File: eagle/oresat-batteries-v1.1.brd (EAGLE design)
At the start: 98.6 x 95.3 mm, 104 parts, among them IC1 74AHC1G08DBV, U1 TCAN330, U10 LTC4412, U2 STM32F042K6, U3 LTC4411, U4 LTC4411, U5 LTC4411, U6 LTC4411, U7 LTC4412, U8 LTC4412, U9 LTC4412, X1 16MHz

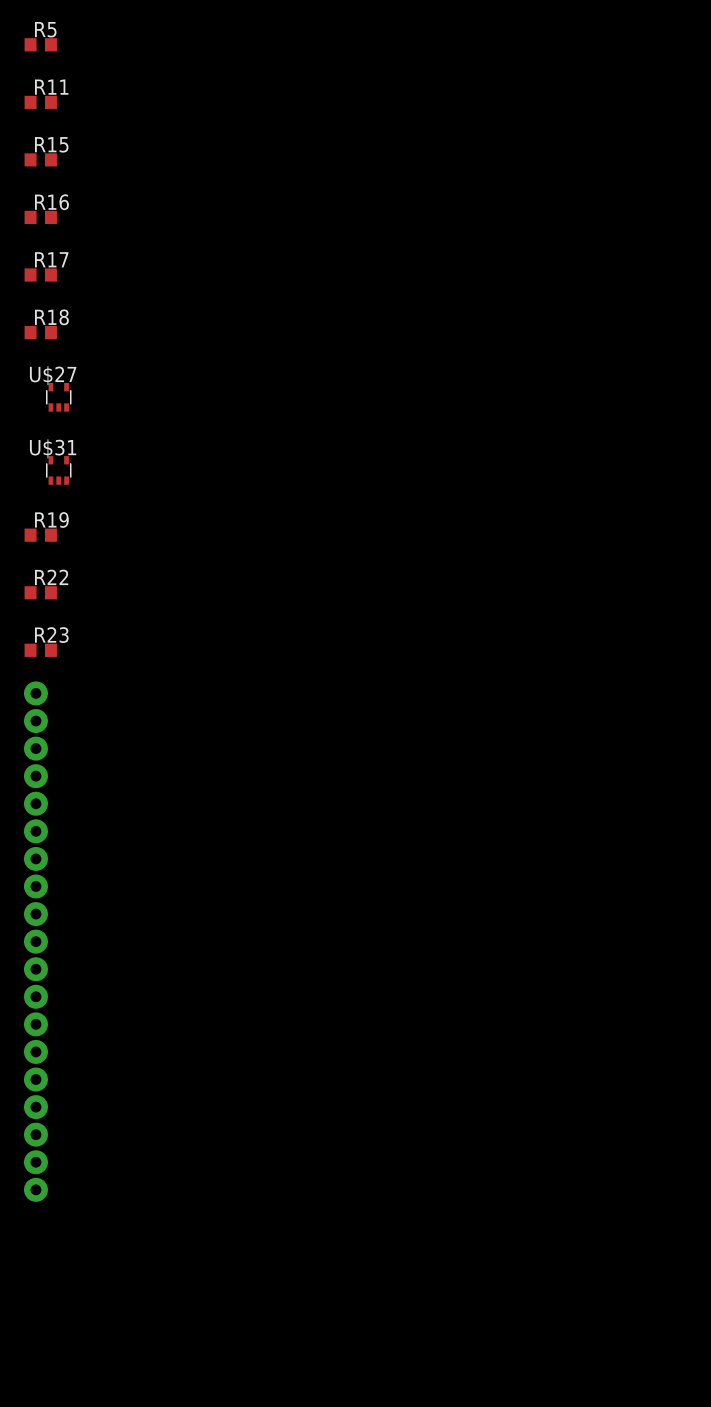
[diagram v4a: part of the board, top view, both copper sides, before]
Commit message: Added double pin header.
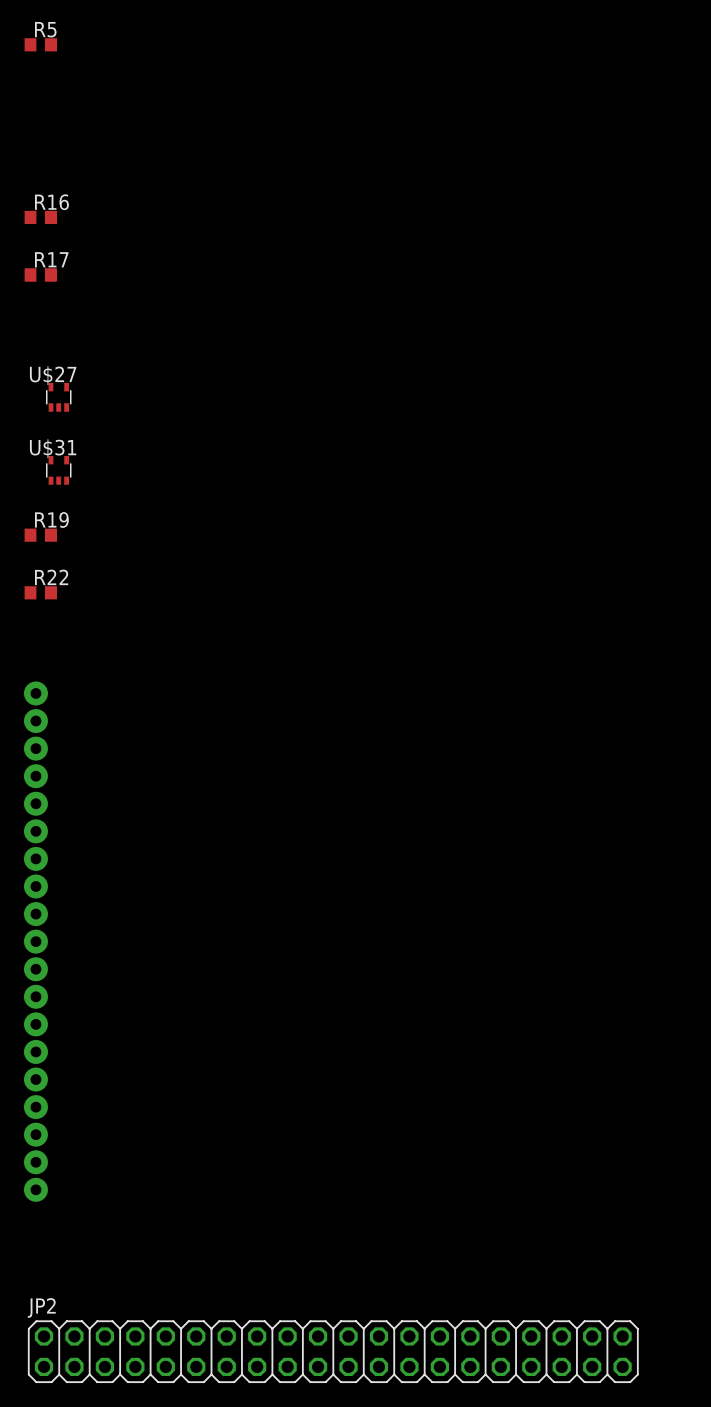
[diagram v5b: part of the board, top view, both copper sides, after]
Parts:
- removed R11, R15, R18, R23: 470k, rcl:R0603
- added JP2: (no value), pinhead:2X20
- R8, R9: value 1.6k -> 4.7k
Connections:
- removed net LOWSHD: C1.1, CF1.11, IC1.1, R14.2, R7.1, U$2.5, U$26.P$1, U$4.P$1
- removed net N$6: C14.1, IC1.5, R14.1
- removed net U10STAT: R5.2, U10.4, U2.26
- removed net U4STAT: R17.2, U2.12, U4.4
- removed net U5STAT: R18.2, U2.13, U5.4
- removed net U8STAT: R4.2, U2.27, U8.4
- new net N$4: U2.18
- new net SPARE1: CF1.19, CF1.20, JP2.19
- new net SPARE10: CF1.37, CF1.38, JP2.37
- new net SPARE11: CF1.39, CF1.40, JP2.39
- new net SPARE2: CF1.21, CF1.22, JP2.21
- new net SPARE3: CF1.23, CF1.24, JP2.23
- new net SPARE4: CF1.25, CF1.26, JP2.25
- new net SPARE5: CF1.27, CF1.28, JP2.27
- new net SPARE6: CF1.29, CF1.30, JP2.29
- new net SPARE7: CF1.31, CF1.32, JP2.31
- new net SPARE8: CF1.33, CF1.34, JP2.33
- new net SPARE9: CF1.35, CF1.36, JP2.35
- new net SYSSHD: C1.1, CF1.17, CF1.18, IC1.1, JP2.17, JP2.18, R14.2, R7.1, U$2.5, U$26.P$1, U$4.P$1
- net 3V3: no longer R11.1, R15.1, R18.1, R23.1
- net BATT+: now also C14.1, IC1.5, R14.1
- net BATT-: no longer R2.1
- net CANH: now also CF1.3, CF1.4, JP2.3, JP2.4; no longer CF1.2
- net CANL: now also CF1.2, JP2.1, JP2.2
- net CHG_CTL: now also CF1.13, CF1.14, JP2.13, JP2.14; no longer CF1.7
- net C_SENSE: now also R2.1, R6.2
- net DCHG_CTL: now also CF1.15, CF1.16, JP2.15, JP2.16; no longer CF1.9
- net GND: now also CF1.11, CF1.12, CF1.5, CF1.6, JP2.11, JP2.5; no longer R6.2
- net U3STAT: now also R17.2, U2.12, U4.4; no longer R23.2, U2.18
- net U6STAT: now also U5.4
- net U7STAT: now also R5.2, U10.4, U2.26; no longer R15.2, U2.10
- net U9STAT: now also R4.2, U2.27, U8.4; no longer R11.2, U2.15
- net VSOLAR: now also CF1.10, CF1.7, CF1.8, CF1.9, JP2.6, JP2.7, JP2.8, JP2.9; no longer CF1.3, CF1.4, CF1.5, CF1.6

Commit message: Fixed most of the issues from design review Sept 25.
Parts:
- removed C16, C17: 10u, rcl:C0805
- removed DEBUG_DNP: (no value), pinhead:2X08
- removed R21, R22: 10k, rcl:R0603
- removed U$1: LM3761, oresat-batteries:SOT23-5
- removed U$2: BQ2970, oresat-batteries:PSOP6
- removed U$21: 4.19, oresat-batteries:RES_HEATER
- removed U$27, U$31: MC74HC1G04DFT1GOSCT, MC74HC1G04DFT1GOSCT:SC70-5
- removed U$49: TP, oresat-batteries:2MM_TP
- added C4, C7: .1u, rcl:C0603
- added D1, D2, D3: CMDD6001, CMMDD6001:SOD323
- added JP1: (no value), pinhead:2X20
- added R11: 4.7k, rcl:R0603
- added R15, R18: 470k, rcl:R0603
- added TP6: TP, oresat-batteries:2MM_TP
- added U12, U13: LTC4412, ltc4412:SOT23-6
- added U14: STM32F042K6, oresat-batteries:QFP32-7X7
- added U15: TCAN330, oresat-batteries:SOT23-8_TI-DCN
- C1, C3: value .1u -> 10u; device rcl:C0603 -> rcl:C0805
- C10, C11: value 100n -> 20p
- C14: value .1u -> 100n
- C15: value 10u -> 100n; device rcl:C0805 -> rcl:C0603
- C2: value .47u -> 10u; device rcl:C0603 -> rcl:C0805
- C8: value 20p -> .1u
- C9: value 20p -> .47u
- JP2: device pinhead:2X20 -> pinhead:2X08
- R1: value 10k -> 330
- R12: value 10k -> 4.7k
- R13: value DNP/0 -> 10k
- R14: value 2.2k -> 470k
- R16: value 470k -> DNP/0
- R20: value 10k -> 4.19; device rcl:R0603 -> oresat-batteries:RES_HEATER
- R3: value .01-.05 -> 10k
- R4: value 470k -> 10k
- R5: value 470k -> 2.2k
- R7: value 330 -> .01-.05
- R8, R9: value 4.7k -> 10k
- U1: value TCAN330 -> LM3761; device oresat-batteries:SOT23-8_TI-DCN -> oresat-batteries:SOT23-5
- U2: value STM32F042K6 -> MC74HC1G04DFT1GOSCT; device oresat-batteries:QFP32-7X7 -> MC74HC1G04DFT1GOSCT:SC70-5
- U3: value LTC4411 -> BQ2970; device ltc4411:SOT23-5-B -> oresat-batteries:PSOP6
- U7: value LTC4412 -> LTC4411; device ltc4412:SOT23-6 -> ltc4411:SOT23-5-B
- U8: value LTC4412 -> MC74HC1G04DFT1GOSCT; device ltc4412:SOT23-6 -> MC74HC1G04DFT1GOSCT:SC70-5
- moved R8 294.6 mm to (-77.2, -210.5)
- moved R19 282.6 mm to (15.5, 56.5)
- moved U2 277.4 mm to (-75.7, -199.0)
- moved R16 273.7 mm to (28.5, 68.5)
- moved JP2 269.1 mm to (1.50, -15.0)
- moved R5 260.1 mm to (8.50, 76.0)
- moved C8 209.9 mm to (-71.1, -120.7)
- moved R14 206.7 mm to (-77.2, -164.8)
- moved R1 202.3 mm to (8.50, 79.0), turned to 180 degrees
- moved R9 197.7 mm to (-60.7, -115.9)
- moved R10 188.2 mm to (-60.7, -111.1)
- moved C9 186.1 mm to (-60.7, -106.3)
- moved U3 184.1 mm to (26.7, 77.3)
- moved R20 153.9 mm to (57.0, 51.0), flipped to the bottom
- moved C1 145.1 mm to (-28.9, -64.8)
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- renumbered C18 to C6, C19 to C5, CF1 to CM1, CF2 to J1, U$10 to TP15, U$11 to TP16, U$12 to TP31, U$13 to Q2, U$14 to Q1, U$15 to TP30, U$16 to TP3, U$17 to TP4, U$18 to TP13, U$19 to TP9, U$20 to Q7, U$22 to TP1, U$23 to TP2, U$24 to Q3, U$25 to TP18, U$26 to TP7, U$28 to TP8, U$29 to Q6, U$3 to B1, U$30 to Q4, U$32 to TP23, U$33 to TP24, U$34 to TP25, U$35 to TP26, U$36 to TP27, U$37 to TP28, U$38 to TP29, U$39 to TP22, U$4 to TP5, U$40 to TP21, U$41 to TP19, U$42 to TP34, U$43 to TP33, U$44 to TP20, U$45 to TP35, U$46 to TP14, U$47 to TP10, U$48 to TP11, U$5 to Q5, U$50 to TP12, U$6 to U11, U$8 to TP32, U$9 to TP17
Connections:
- removed net 3V3: C10.1, C11.1, C12.1, C13.1, C5.1, C6.1, DEBUG_DNP.1, DEBUG_DNP.2, J1.2, L1.1, Q7.P$5, Q7.P$6, Q7.P$7, Q7.P$8, Q7.P$9, R10.2, R16.1, R17.1, R4.1, R5.1, R8.2, R9.2, TP22.P$1, TP29.P$1, TP30.P$1, U$1.4, U1.3, U2.1, U2.17, U2.5
- removed net BATT+: B1.POS, C14.1, C15.1, C16.1, C3.1, IC1.5, Q3.5, Q3.6, Q3.7, Q3.8, Q4.5, Q4.6, Q4.7, Q4.8, R14.1, R19.2, R21.2, R22.2, R7.2, TP12.P$1, U$1.1, U$27.3, U$31.3, U11.10, U4.5, U6.5, U7.1, U9.1
- new net 3.3V: C12.1, C13.1, C14.1, C15.1, C5.1, C6.1, J1.2, JP2.1, JP2.2, L1.1, Q7.P$5, Q7.P$6, Q7.P$7, Q7.P$8, Q7.P$9, R11.2, R12.2, R13.2, R14.1, R15.1, R17.1, R18.1, TP22.P$1, TP29.P$1, TP30.P$1, U1.4, U14.1, U14.17, U14.5, U15.3
- new net N$10: D3.2, R4.1, U2.2
- new net N$6: D1.1, JP1.18
- new net N$9: D2.1, JP1.16
- new net VBATT: B1.POS, C1.1, C2.1, C7.1, C8.1, IC1.5, Q3.5, Q3.6, Q3.7, Q3.8, Q4.5, Q4.6, Q4.7, Q4.8, R1.2, R2.2, R4.2, R6.1, R8.2, TP12.P$1, U1.1, U10.1, U11.10, U2.3, U6.5, U7.5, U8.3, U9.1
- net 4411MB: now also U7.1; no longer U6.1
- net 4411_MT: now also U4.5, U6.1; no longer U3.5, U4.1
- net ALERT: now also R13.1, R16.2; no longer R10.1, R13.2
- net BATT-: now also U3.4; no longer U$2.4
- net BQVMIN: now also R5.1, U3.6; no longer R6.1, U$2.6
- net CANH: now also JP1.3, JP1.4, JP2.13, JP2.14, U15.7; no longer DEBUG_DNP.13, DEBUG_DNP.14, JP2.3, JP2.4, U1.7
- net CANL: now also JP1.1, JP1.2, JP2.11, JP2.12, U15.6; no longer DEBUG_DNP.11, DEBUG_DNP.12, JP2.1, JP2.2, U1.6
- net CAN_EN: now also U14.20, U15.5; no longer U1.5, U2.20
- net CAN_LSTN: now also U14.19, U15.8; no longer U1.8, U2.19
- net CAN_RX: now also U14.21, U15.4; no longer U1.4, U2.21
- net CAN_TX: now also U14.22, U15.1; no longer U1.1, U2.22
- net CHG_CTL: now also D3.1, JP1.13, JP1.14; no longer JP2.13, JP2.14, R22.1, U$27.2
- net CHG_SHD: now also U2.4, U7.3; no longer U$27.4, U3.3
- net COUT: now also U3.2; no longer U$2.2
- net C_SENSE: now also R5.2, R7.2, R9.1; no longer R2.1, R3.2, R6.2
- net DCHG_CTL: now also D2.2, JP1.15, R8.1, U8.2; no longer JP2.15, JP2.16, R19.1, U$31.2
- net DSCHG_SHD: now also U12.3, U13.3, U8.4; no longer U$31.4, U7.3, U8.3
- net GND: now also C4.2, C7.2, JP1.11, JP1.5, JP2.15, JP2.16, R19.1, R20.V-, R7.1, U12.2, U13.2, U14.16, U14.32, U15.2, U2.5, U8.5; no longer C16.2, C17.2, DEBUG_DNP.15, DEBUG_DNP.16, JP2.11, JP2.5, R12.1, R20.1, U$1.2, U$21.V-, U$27.5, U$31.5, U2.16, U2.32, U3.2, U8.2
- net HEAT: now also U14.7; no longer U2.7
- net N$1: now also U1.5; no longer U$1.5
- net N$11: now also U12.1, U9.6; no longer U10.1, U7.6
- net N$12: now also U9.5; no longer U7.5
- net N$13: now also R20.V+; no longer U$21.V+
- net N$16: now also U13.5; no longer U8.5
- net N$18: now also U10.6, U13.1; no longer U8.1, U9.6
- net N$19: now also U10.5; no longer U9.5
- net N$2: now also R19.2, U14.31; no longer R12.2, U2.31
- net N$3: now also R10.1, R9.2; no longer R1.1, R2.2
- net N$4: now also U14.18; no longer U2.18
- net N$5: now also U3.3; no longer U$2.3
- net N$7: now also C3.1, R2.1, R3.2, U1.3; no longer C17.1, R20.2, R21.1, U$1.3
- net N$8: now also U12.5; no longer U10.5
- net NRESET: now also U14.4; no longer U2.4
- net OSC_IN: now also C10.1, U14.2; no longer C8.1, U2.2
- net OSC_OUT: now also C11.1, U14.3; no longer C9.1, U2.3
- net REG: now also C9.1; no longer C2.1
- net SCL: now also R11.1, U14.29; no longer R8.1, U2.29
- net SDA: now also R12.1, U14.30; no longer R9.1, U2.30
- net SPARE1: now also JP1.19; no longer JP2.19
- net SPARE10: now also JP1.37; no longer JP2.37
- net SPARE11: now also JP1.39; no longer JP2.39
- net SPARE2: now also JP1.21; no longer JP2.21
- net SPARE3: now also JP1.23; no longer JP2.23
- net SPARE4: now also JP1.25; no longer JP2.25
- net SPARE5: now also JP1.27; no longer JP2.27
- net SPARE6: now also JP1.29; no longer JP2.29
- net SPARE7: now also JP1.31; no longer JP2.31
- net SPARE8: now also JP1.33; no longer JP2.33
- net SPARE9: now also JP1.35; no longer JP2.35
- net STC_IO: now also R16.1, U14.28; no longer R13.1, U2.28
- net STM_DEBUG: now also U14.6; no longer U2.6
- net SWCLK: now also U14.24; no longer U2.24
- net SWDIO: now also U14.23; no longer U2.23
- net SYSSHD: now also C4.1, D1.2, JP1.17, R1.1, R6.2, U3.5; no longer C1.1, JP2.17, JP2.18, R14.2, R7.1, U$2.5
- net THRM: now also R10.2; no longer R1.2
- net U3STAT: now also R18.2, U14.12, U6.4; no longer R17.2, U2.12, U3.4
- net U6STAT: now also R17.2, U14.11, U7.4; no longer R16.2, U2.11, U6.4
- net U7STAT: now also R15.2, U12.4, U14.26, U9.4; no longer R5.2, U10.4, U2.26, U7.4
- net U9STAT: now also R14.2, U10.4, U13.4, U14.27; no longer R4.2, U2.27, U8.4, U9.4
- net USART2_RX: now also JP2.5, JP2.6, U14.9; no longer DEBUG_DNP.5, DEBUG_DNP.6, U2.9
- net USART2_TX: now also JP2.3, JP2.4, U14.8; no longer DEBUG_DNP.3, DEBUG_DNP.4, U2.8
- net VSOLAR: now also JP1.6, JP1.7, JP1.8, JP1.9, JP2.10, TP6.P$1, U12.6, U13.6, U4.1; no longer DEBUG_DNP.10, DEBUG_DNP.7, DEBUG_DNP.8, DEBUG_DNP.9, JP2.6, U$49.P$1, U10.6, U3.1, U8.6

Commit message: Cosmetics.
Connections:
- new net 5V: C8.1, U11.10
- net VBATT: no longer C8.1, U11.10
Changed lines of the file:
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@@
 <contactref element="TP12" pad="P$1"/>
 <contactref element="R1" pad="2"/>
-<contactref element="U11" pad="10"/>
-<contactref element="C8" pad="1"/>
 <contactref element="IC1" pad="5"/>
 <contactref element="C7" pad="1"/>
@@
 <wire x1="-74.725" y1="-131.225" x2="-75.375" y2="-131.225" width="0" layer="19" extent="1-1"/>
 <wire x1="-75.35" y1="-125.19" x2="-75.375" y2="-131.225" width="0" layer="19" extent="1-1"/>
-<wire x1="-71.95" y1="-120.7" x2="-75.35" y2="-125.19" width="0" layer="19" extent="1-1"/>
-<wire x1="-60.3" y1="-102.175" x2="-71.95" y2="-120.7" width="0" layer="19" extent="1-1"/>
-<wire x1="-48.45" y1="-97.85" x2="-60.3" y2="-102.175" width="0" layer="19" extent="1-1"/>
+<wire x1="-48.45" y1="-97.85" x2="-75.35" y2="-125.19" width="0" layer="19" extent="1-1"/>
 <wire x1="-38.05" y1="-97.85" x2="-48.45" y2="-97.85" width="0" layer="19" extent="1-1"/>
 <wire x1="-28.55" y1="-81.1" x2="-38.05" y2="-97.85" width="0" layer="19" extent="1-1"/>
@@
 <wire x1="-75.7" y1="-199.85" x2="-78.05" y2="-215.3" width="0" layer="19" extent="1-1"/>
 </signal>
+<signal name="5V">
+<contactref element="U11" pad="10"/>
+<contactref element="C8" pad="1"/>
+<wire x1="-60.3" y1="-102.175" x2="-71.95" y2="-120.7" width="0" layer="19" extent="1-1"/>
+</signal>
 </signals>

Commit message: Cosmetics again.
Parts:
- removed TP10: TP, oresat-batteries:2MM_TP
- moved TP20 80.1 mm to (-77.6, -331.4)
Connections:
- net STC_IO renamed MAX_IO
- removed net N$10: D3.2, R4.1, U2.2
- removed net N$9: D2.1, JP1.16
- new net !SHUTDOWN: CM1.7, CM1.8, JP1.7
- new net TO_CHG: D3.2, R4.1, U14.26, U2.2
- new net TO_DCHG: D2.2, R8.1, U14.27, U8.2
- net BATT-: now also TP20.P$1
- net CHG_CTL: now also CM1.15, CM1.16, JP1.15, JP1.16; no longer CM1.13, CM1.14, JP1.13, JP1.14
- net CHG_SHD: no longer TP10.P$1
- net DCHG_CTL: now also CM1.17, CM1.18, D2.1, JP1.17, JP1.18; no longer CM1.15, CM1.16, D2.2, JP1.15, R8.1, U8.2
- net GND: now also CM1.10, CM1.9, JP1.10, JP1.6, JP1.9; no longer CM1.11, CM1.12, JP1.11
- net N$16: now also U13.6
- net N$6: now also JP1.8; no longer JP1.18
- net SYSSHD: no longer CM1.17, CM1.18, JP1.17
- net U7STAT: now also U14.14; no longer U14.26
- net U9STAT: now also U14.15; no longer U14.27
- net USART2_RX: no longer TP20.P$1
- net VSOLAR: now also CM1.11, CM1.12, CM1.13, CM1.14, JP1.11, JP1.12, JP1.13, JP1.14; no longer CM1.10, CM1.7, CM1.8, CM1.9, JP1.6, JP1.7, JP1.8, JP1.9, U13.6
